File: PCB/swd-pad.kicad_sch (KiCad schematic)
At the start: 1 part, among them J7 OroConn6p

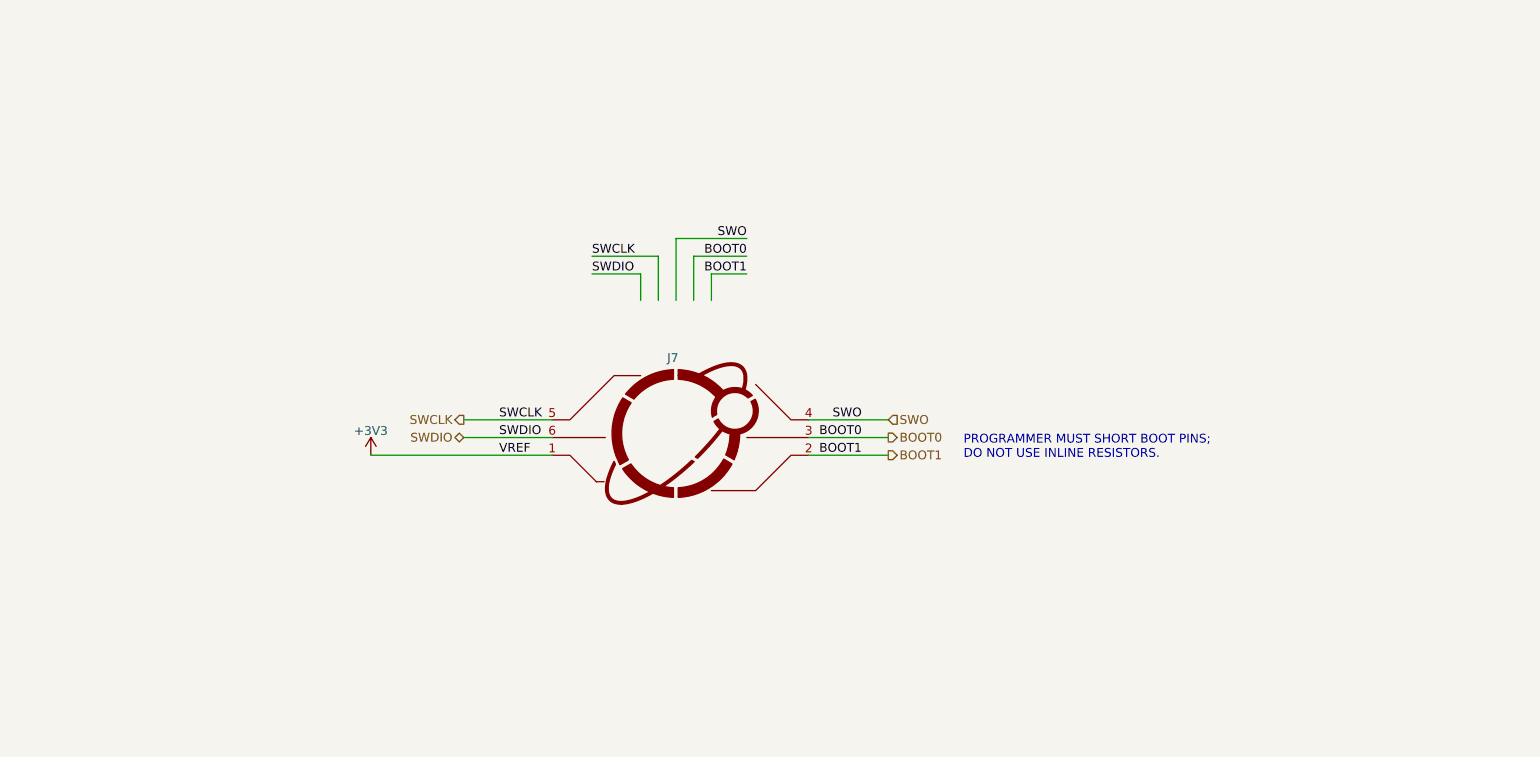
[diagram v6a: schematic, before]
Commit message: eliminate programmer SWD pad in lieu of edge connector / minie (closes #40, closes #42)
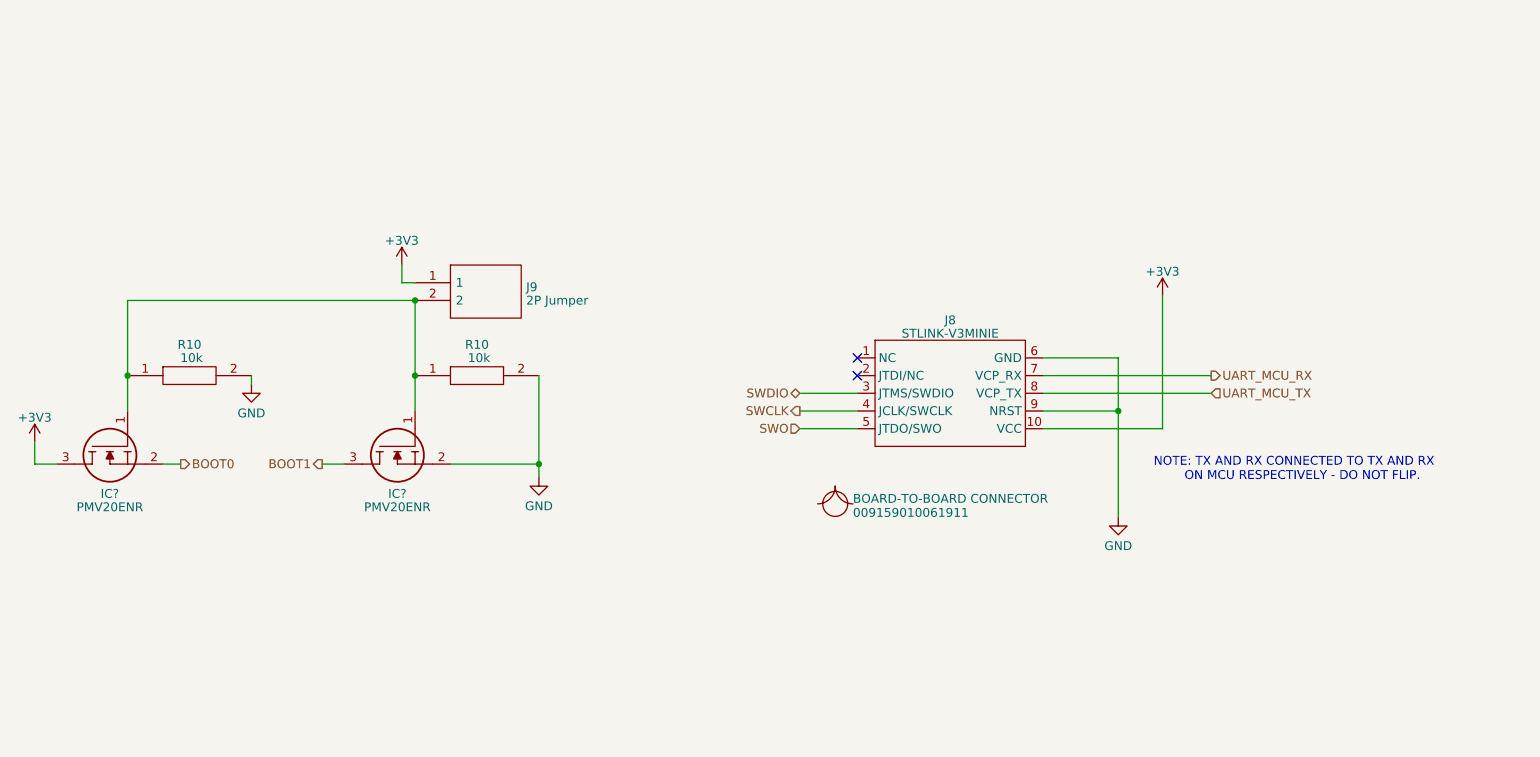
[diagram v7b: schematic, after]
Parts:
- removed J7: OroConn6p, Oro Footprints:OroConn6p_WithMounts, symbol Oro:OroConn6p
- added B2: 009159010061911, symbol Oro:BOM Part
- added IC? (x2): PMV20ENR, SamacSys_Parts:SOT95P230X110-3N, symbol SamacSys_Parts:CSD13380F3T
- added J8: STLINK-V3MINIE, Oro Footprints:009159010061911, symbol Oro:STLINK-V3MINIE
- added J9: 2P Jumper, HDRV2W67P0X254_1X2_508X241X1082P, symbol SamacSys_Parts:10129378-902003BLF
- added R10 (x2): 10k, RESC1005X40N, symbol SamacSys_Parts:RK73H1ETTP1002F
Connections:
- net +3V3: now also IC?.3, J8.10 (VCC), J9.1
- net BOOT0: now also IC?.2
- net BOOT1: now also IC?.3
- net SWCLK: now also J8.4 (JCLK/SWCLK)
- net SWDIO: now also J8.3 (JTMS/SWDIO)
- net SWO: now also J8.5 (JTDO/SWO)
- new net: IC?.1, IC?.1, J9.2, R10.1, R10.1
- new net GND: IC?.2, J8.6 (GND), J8.9 (NRST), R10.2, R10.2
- new net UART_MCU_RX: J8.7 (VCP_RX)
- new net UART_MCU_TX: J8.8 (VCP_TX)
- no-connect marks 0 -> 2
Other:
- note added: "NOTE: TX AND RX CONNECTED TO TX AND RX ON MCU RESPECTIVELY - DO NOT FLIP."
- note removed: "PROGRAMMER MUST SHORT BOOT PINS; DO NOT USE INLINE RESISTORS."

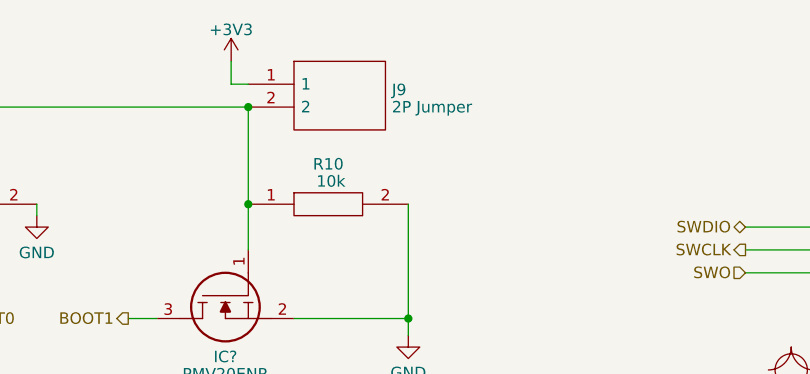
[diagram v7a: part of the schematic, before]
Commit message: switch out linear regular for one with larger max current (closes #43)
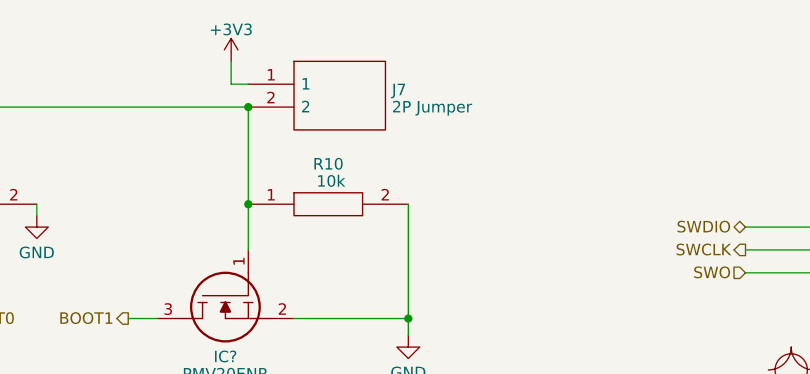
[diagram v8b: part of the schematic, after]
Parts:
- renumbered J9 to J7
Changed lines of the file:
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@@
   (symbol (lib_id "power:+3V3") (at 103.505 82.55 0) (unit 1)
     (in_bom yes) (on_board yes) (dnp no) (fields_autoplaced)
-    (property "Reference" "#PWR081" (at 103.505 86.36 0)
+    (property "Reference" "#PWR080" (at 103.505 86.36 0)
       (effects (font (size 1.27 1.27)) hide)
     )
@@
       (project "OroLink"
         (path "/e89dcd22-1250-4a5b-b778-1c95a0dd623d/259c9346-7ad9-40c3-9e14-9b19afc78ddf"
-          (reference "#PWR081") (unit 1)
+          (reference "#PWR080") (unit 1)
         )
       )
@@
   (symbol (lib_id "power:GND") (at 81.915 99.695 0) (unit 1)
     (in_bom yes) (on_board yes) (dnp no) (fields_autoplaced)
-    (property "Reference" "#PWR084" (at 81.915 106.045 0)
+    (property "Reference" "#PWR079" (at 81.915 106.045 0)
       (effects (font (size 1.27 1.27)) hide)
     )
@@
       (project "OroLink"
         (path "/e89dcd22-1250-4a5b-b778-1c95a0dd623d/259c9346-7ad9-40c3-9e14-9b19afc78ddf"
-          (reference "#PWR084") (unit 1)
+          (reference "#PWR079") (unit 1)
         )
       )
@@
   (symbol (lib_id "power:+3V3") (at 50.8 107.95 0) (unit 1)
     (in_bom yes) (on_board yes) (dnp no) (fields_autoplaced)
-    (property "Reference" "#PWR087" (at 50.8 111.76 0)
+    (property "Reference" "#PWR078" (at 50.8 111.76 0)
       (effects (font (size 1.27 1.27)) hide)
     )
@@
       (project "OroLink"
         (path "/e89dcd22-1250-4a5b-b778-1c95a0dd623d/259c9346-7ad9-40c3-9e14-9b19afc78ddf"
-          (reference "#PWR087") (unit 1)
+          (reference "#PWR078") (unit 1)
         )
       )
@@
   (symbol (lib_id "SamacSys_Parts:10129378-902003BLF") (at 105.41 85.09 0) (unit 1)
     (in_bom yes) (on_board yes) (dnp no) (fields_autoplaced)
-    (property "Reference" "J9" (at 121.3612 85.7163 0)
+    (property "Reference" "J7" (at 121.3612 85.7163 0)
       (effects (font (size 1.27 1.27)) (justify left))
     )
@@
       (project "OroLink"
         (path "/e89dcd22-1250-4a5b-b778-1c95a0dd623d/259c9346-7ad9-40c3-9e14-9b19afc78ddf"
-          (reference "J9") (unit 1)
+          (reference "J7") (unit 1)
         )
       )
@@
         )
         (path "/e89dcd22-1250-4a5b-b778-1c95a0dd623d/259c9346-7ad9-40c3-9e14-9b19afc78ddf"
-          (reference "IC16") (unit 1)
+          (reference "IC13") (unit 1)
         )
       )
@@
         )
         (path "/e89dcd22-1250-4a5b-b778-1c95a0dd623d/259c9346-7ad9-40c3-9e14-9b19afc78ddf"
-          (reference "R62") (unit 1)
+          (reference "R57") (unit 1)
         )
       )
@@
   (symbol (lib_id "power:GND") (at 206.375 118.745 0) (unit 1)
     (in_bom yes) (on_board yes) (dnp no) (fields_autoplaced)
-    (property "Reference" "#PWR089" (at 206.375 125.095 0)
+    (property "Reference" "#PWR082" (at 206.375 125.095 0)
       (effects (font (size 1.27 1.27)) hide)
     )
@@
       (project "OroLink"
         (path "/e89dcd22-1250-4a5b-b778-1c95a0dd623d/259c9346-7ad9-40c3-9e14-9b19afc78ddf"
-          (reference "#PWR089") (unit 1)
+          (reference "#PWR082") (unit 1)
         )
       )
@@
         )
         (path "/e89dcd22-1250-4a5b-b778-1c95a0dd623d/259c9346-7ad9-40c3-9e14-9b19afc78ddf"
-          (reference "R61") (unit 1)
+          (reference "R58") (unit 1)
         )
       )
@@
   (symbol (lib_id "power:GND") (at 123.19 113.03 0) (unit 1)
     (in_bom yes) (on_board yes) (dnp no) (fields_autoplaced)
-    (property "Reference" "#PWR083" (at 123.19 119.38 0)
+    (property "Reference" "#PWR081" (at 123.19 119.38 0)
       (effects (font (size 1.27 1.27)) hide)
     )
@@
       (project "OroLink"
         (path "/e89dcd22-1250-4a5b-b778-1c95a0dd623d/259c9346-7ad9-40c3-9e14-9b19afc78ddf"
-          (reference "#PWR083") (unit 1)
+          (reference "#PWR081") (unit 1)
         )
       )
@@
   (symbol (lib_id "power:+3V3") (at 212.725 86.995 0) (unit 1)
     (in_bom yes) (on_board yes) (dnp no) (fields_autoplaced)
-    (property "Reference" "#PWR091" (at 212.725 90.805 0)
+    (property "Reference" "#PWR083" (at 212.725 90.805 0)
       (effects (font (size 1.27 1.27)) hide)
     )
@@
       (project "OroLink"
         (path "/e89dcd22-1250-4a5b-b778-1c95a0dd623d/259c9346-7ad9-40c3-9e14-9b19afc78ddf"
-          (reference "#PWR091") (unit 1)
+          (reference "#PWR083") (unit 1)
         )
       )
@@
         )
         (path "/e89dcd22-1250-4a5b-b778-1c95a0dd623d/259c9346-7ad9-40c3-9e14-9b19afc78ddf"
-          (reference "IC17") (unit 1)
-        )
-      )
+          (reference "IC12") (unit 1)
+        )
+      )
